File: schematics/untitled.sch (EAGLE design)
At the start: 9 parts, among them IC2 L293D

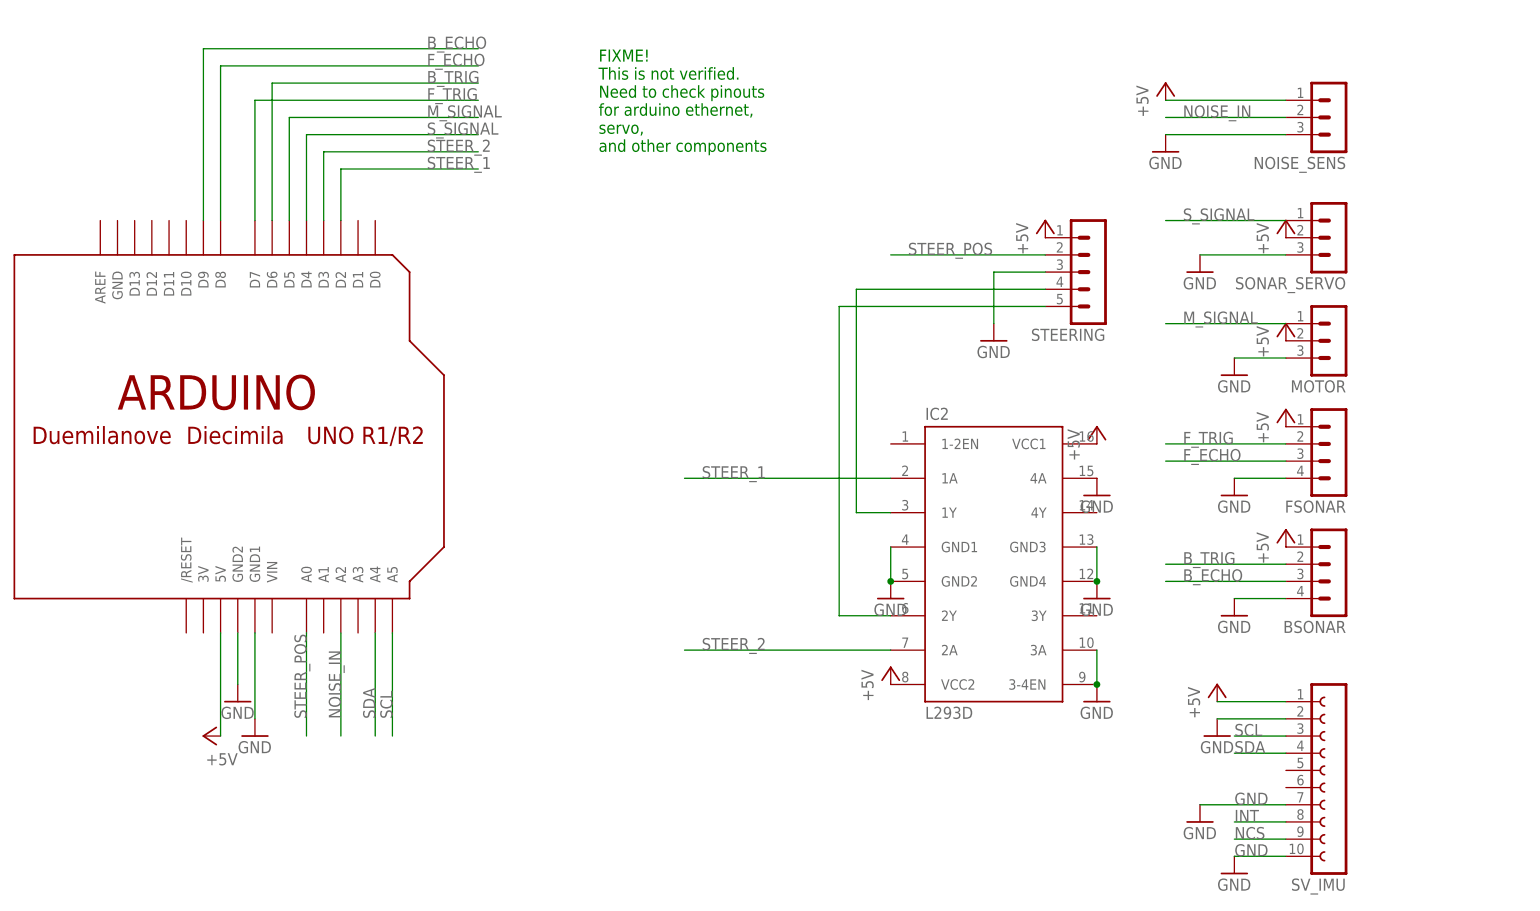
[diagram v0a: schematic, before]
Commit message: Changed schematics and pcb - new connectors, new arduino pins
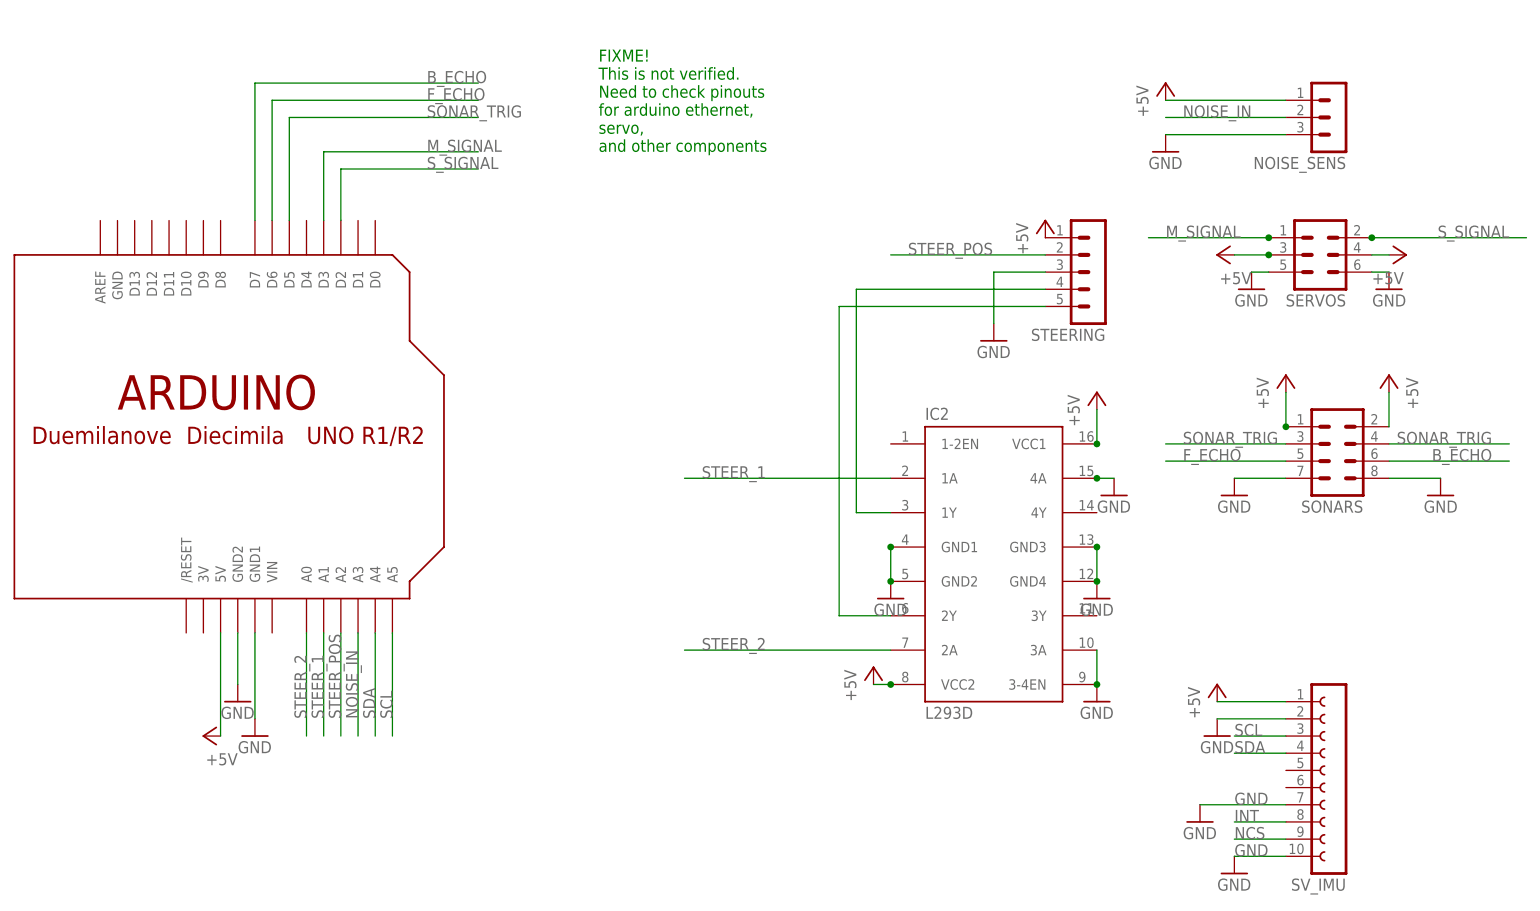
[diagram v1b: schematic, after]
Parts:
- removed BSONAR, FSONAR: (no value), con-lstb:MA04-1
- removed MOTOR, SONAR_SERVO: (no value), con-lstb:MA03-1
- added SERVOS: (no value), con-lstb:MA03-2
- added SONARS: (no value), con-lstb:MA04-2
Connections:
- removed net B_TRIG: BSONAR.2, U$1.D6
- removed net F_TRIG: FSONAR.2, U$1.D7
- new net SONAR_TRIG: SONARS.3, SONARS.4, U$1.D5
- net +5V: now also SERVOS.3, SERVOS.4, SONARS.1, SONARS.2; no longer BSONAR.1, FSONAR.1, MOTOR.2, SONAR_SERVO.2
- net B_ECHO: now also SONARS.6, U$1.D7; no longer BSONAR.3, U$1.D9
- net F_ECHO: now also SONARS.5, U$1.D6; no longer FSONAR.3, U$1.D8
- net GND: now also SERVOS.5, SERVOS.6, SONARS.7, SONARS.8; no longer BSONAR.4, FSONAR.4, MOTOR.3, SONAR_SERVO.3
- net M_SIGNAL: now also SERVOS.1, U$1.D3; no longer MOTOR.1, U$1.D5
- net NOISE_IN: now also U$1.A3; no longer U$1.A2
- net STEER_1: now also U$1.A1; no longer U$1.D2
- net STEER_2: now also U$1.A0; no longer U$1.D3
- net STEER_POS: now also U$1.A2; no longer U$1.A0
- net S_SIGNAL: now also SERVOS.2, U$1.D2; no longer SONAR_SERVO.1, U$1.D4

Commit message: Updated schematics for 2 sonars. Added sonar test. Added makefiles
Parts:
- added D1, D2: 1N4148DO35-7, diode:1N4148DO35-7
- added R1: (no value), rcl:R-EU_0204/2V
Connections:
- removed net SONAR_TRIG: SONARS.3, SONARS.4, U$1.D5
- new net B_TRIG: SONARS.4, U$1.D6
- new net ECHO: D1.C, D2.C, R1.2, U$1.D7
- new net F_TRIG: SONARS.3, U$1.D5
- net B_ECHO: now also D2.A; no longer U$1.D7
- net F_ECHO: now also D1.A; no longer U$1.D6
- net GND: now also R1.1
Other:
- note added: "do not use sonars at the same time"
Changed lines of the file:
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@@
 <part name="SONARS" library="con-lstb" deviceset="MA04-2" device=""/>
 <part name="SERVOS" library="con-lstb" deviceset="MA03-2" device=""/>
+<part name="D1" library="diode" deviceset="1N4148" device="DO35-7"/>
+<part name="D2" library="diode" deviceset="1N4148" device="DO35-7"/>
+<part name="R1" library="rcl" deviceset="R-EU_" device="0204/2V"/>
+<part name="GND4" library="supply1" deviceset="GND" device=""/>
 </parts>
 <sheets>
@@
 servo,
 and other components</text>
+<text x="-2.54" y="124.46" size="1.778" layer="91">do not use sonars at the same time</text>
 </plain>
 <instances>
@@
 <instance part="SONARS" gate="G$1" x="160.02" y="60.96" rot="R180"/>
 <instance part="SERVOS" gate="1" x="157.48" y="91.44" rot="R180"/>
+<instance part="D1" gate="G$1" x="15.24" y="116.84" rot="R180"/>
+<instance part="D2" gate="G$1" x="15.24" y="114.3" rot="R180"/>
+<instance part="R1" gate="G$1" x="-5.08" y="111.76"/>
+<instance part="GND4" gate="1" x="-10.16" y="109.22"/>
 </instances>
 <busses>
@@
 <pinref part="GND1" gate="1" pin="GND"/>
 </segment>
+<segment>
+<pinref part="R1" gate="G$1" pin="1"/>
+<pinref part="GND4" gate="1" pin="GND"/>
+</segment>
 </net>
 <net name="S_SIGNAL" class="0">
@@
 </segment>
 <segment>
-<label x="25.4" y="114.3" size="1.778" layer="95"/>
-<pinref part="U$1" gate="G$1" pin="D6"/>
-<wire x1="2.54" y1="114.3" x2="33.02" y2="114.3" width="0.1524" layer="91"/>
-<wire x1="2.54" y1="96.52" x2="2.54" y2="114.3" width="0.1524" layer="91"/>
+<pinref part="D1" gate="G$1" pin="A"/>
+<wire x1="17.78" y1="116.84" x2="33.02" y2="116.84" width="0.1524" layer="91"/>
+<label x="25.4" y="116.84" size="1.778" layer="95"/>
 </segment>
 </net>
@@
 </segment>
 <segment>
-<pinref part="U$1" gate="G$1" pin="D7"/>
-<wire x1="0" y1="96.52" x2="0" y2="116.84" width="0.1524" layer="91"/>
-<wire x1="0" y1="116.84" x2="33.02" y2="116.84" width="0.1524" layer="91"/>
-<label x="25.4" y="116.84" size="1.778" layer="95"/>
+<wire x1="17.78" y1="114.3" x2="33.02" y2="114.3" width="0.1524" layer="91"/>
+<pinref part="D2" gate="G$1" pin="A"/>
+<label x="25.4" y="114.3" size="1.778" layer="95"/>
 </segment>
 </net>
@@
 </segment>
 </net>
-<net name="SONAR_TRIG" class="0">
+<net name="F_TRIG" class="0">
 <segment>
 <wire x1="152.4" y1="63.5" x2="134.62" y2="63.5" width="0.1524" layer="91"/>
@@
 </segment>
 <segment>
+<pinref part="U$1" gate="G$1" pin="D5"/>
+<wire x1="5.08" y1="96.52" x2="5.08" y2="109.22" width="0.1524" layer="91"/>
+<wire x1="5.08" y1="109.22" x2="33.02" y2="109.22" width="0.1524" layer="91"/>
+<label x="25.4" y="109.22" size="1.778" layer="95"/>
+</segment>
+</net>
+<net name="B_TRIG" class="0">
+<segment>
 <wire x1="167.64" y1="63.5" x2="185.42" y2="63.5" width="0.1524" layer="91"/>
 <label x="182.88" y="63.5" size="1.778" layer="95" rot="MR0"/>
@@
 </segment>
 <segment>
-<pinref part="U$1" gate="G$1" pin="D5"/>
-<wire x1="5.08" y1="96.52" x2="5.08" y2="111.76" width="0.1524" layer="91"/>
 <wire x1="5.08" y1="111.76" x2="33.02" y2="111.76" width="0.1524" layer="91"/>
 <label x="25.4" y="111.76" size="1.778" layer="95"/>
-</segment>
-</net>
+<pinref part="U$1" gate="G$1" pin="D6"/>
+<wire x1="5.08" y1="111.76" x2="2.54" y2="111.76" width="0.1524" layer="91"/>
+<wire x1="2.54" y1="111.76" x2="2.54" y2="96.52" width="0.1524" layer="91"/>
+</segment>
+</net>
+<net name="ECHO" class="0">
+<segment>
+<wire x1="2.54" y1="114.3" x2="12.7" y2="114.3" width="0.1524" layer="91"/>
+<pinref part="D2" gate="G$1" pin="C"/>
+<pinref part="U$1" gate="G$1" pin="D7"/>
+<wire x1="0" y1="96.52" x2="0" y2="111.76" width="0.1524" layer="91"/>
+<wire x1="0" y1="111.76" x2="0" y2="114.3" width="0.1524" layer="91"/>
+<wire x1="0" y1="114.3" x2="0" y2="116.84" width="0.1524" layer="91"/>
+<wire x1="0" y1="116.84" x2="12.7" y2="116.84" width="0.1524" layer="91"/>
+<pinref part="D1" gate="G$1" pin="C"/>
+<label x="0" y="99.06" size="1.778" layer="95" rot="R90"/>
+<wire x1="2.54" y1="114.3" x2="0" y2="114.3" width="0.1524" layer="91"/>
+<junction x="0" y="114.3"/>
+<pinref part="R1" gate="G$1" pin="2"/>
+<junction x="0" y="111.76"/>
+</segment>
+</net>

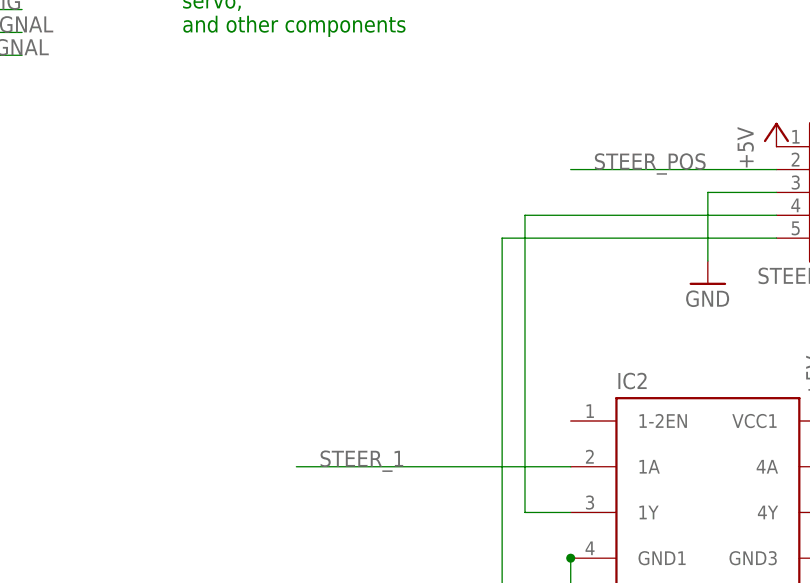
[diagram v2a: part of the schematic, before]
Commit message: Added power smoothing capacitor
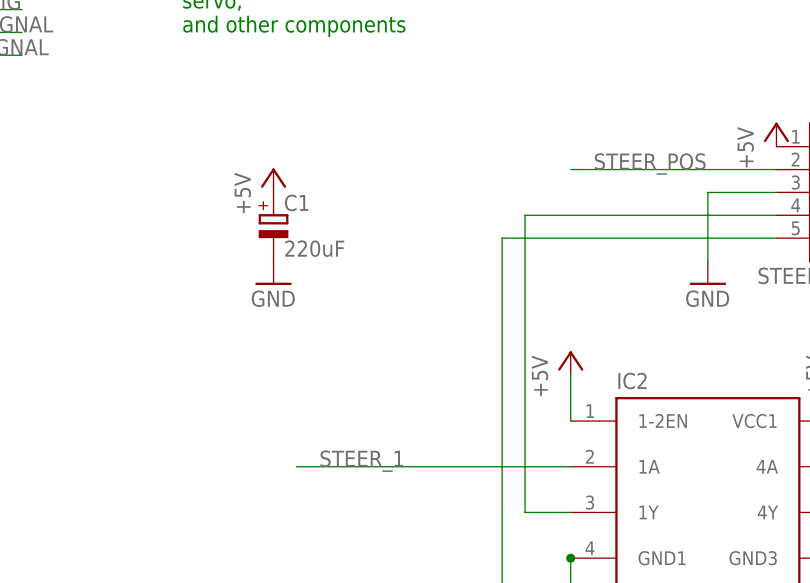
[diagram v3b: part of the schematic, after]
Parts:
- added C1: 220uF, rcl:CPOL-EUE5-8.5
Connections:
- net +5V: now also C1.+, IC2.1-2EN
- net GND: now also C1.-
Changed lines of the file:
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@@
 <part name="R1" library="rcl" deviceset="R-EU_" device="0204/2V"/>
 <part name="GND4" library="supply1" deviceset="GND" device=""/>
+<part name="P+11" library="supply1" deviceset="+5V" device=""/>
+<part name="C1" library="rcl" deviceset="CPOL-EU" device="E5-8.5" value="220uF"/>
+<part name="GND17" library="supply1" deviceset="GND" device=""/>
+<part name="P+12" library="supply1" deviceset="+5V" device=""/>
 </parts>
 <sheets>
@@
 <instance part="R1" gate="G$1" x="-5.08" y="111.76"/>
 <instance part="GND4" gate="1" x="-10.16" y="109.22"/>
+<instance part="P+11" gate="1" x="93.98" y="71.12"/>
+<instance part="C1" gate="G$1" x="60.96" y="86.36"/>
+<instance part="GND17" gate="1" x="60.96" y="78.74"/>
+<instance part="P+12" gate="1" x="60.96" y="91.44"/>
 </instances>
 <busses>
@@
 <pinref part="GND4" gate="1" pin="GND"/>
 </segment>
+<segment>
+<pinref part="C1" gate="G$1" pin="-"/>
+<pinref part="GND17" gate="1" pin="GND"/>
+</segment>
 </net>
 <net name="S_SIGNAL" class="0">
@@
 <pinref part="P+10" gate="1" pin="+5V"/>
 </segment>
-</net>
+<segment>
+<pinref part="IC2" gate="G$1" pin="1-2EN"/>
+<pinref part="P+11" gate="1" pin="+5V"/>
+<wire x1="93.98" y1="68.58" x2="93.98" y2="63.5" width="0.1524" layer="91"/>
+</segment>
+<segment>
+<pinref part="C1" gate="G$1" pin="+"/>
+<pinref part="P+12" gate="1" pin="+5V"/>
+</segment>
+</net>
